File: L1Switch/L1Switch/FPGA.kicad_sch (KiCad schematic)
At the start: 4 parts, among them U1 XC7A15T-FTG256

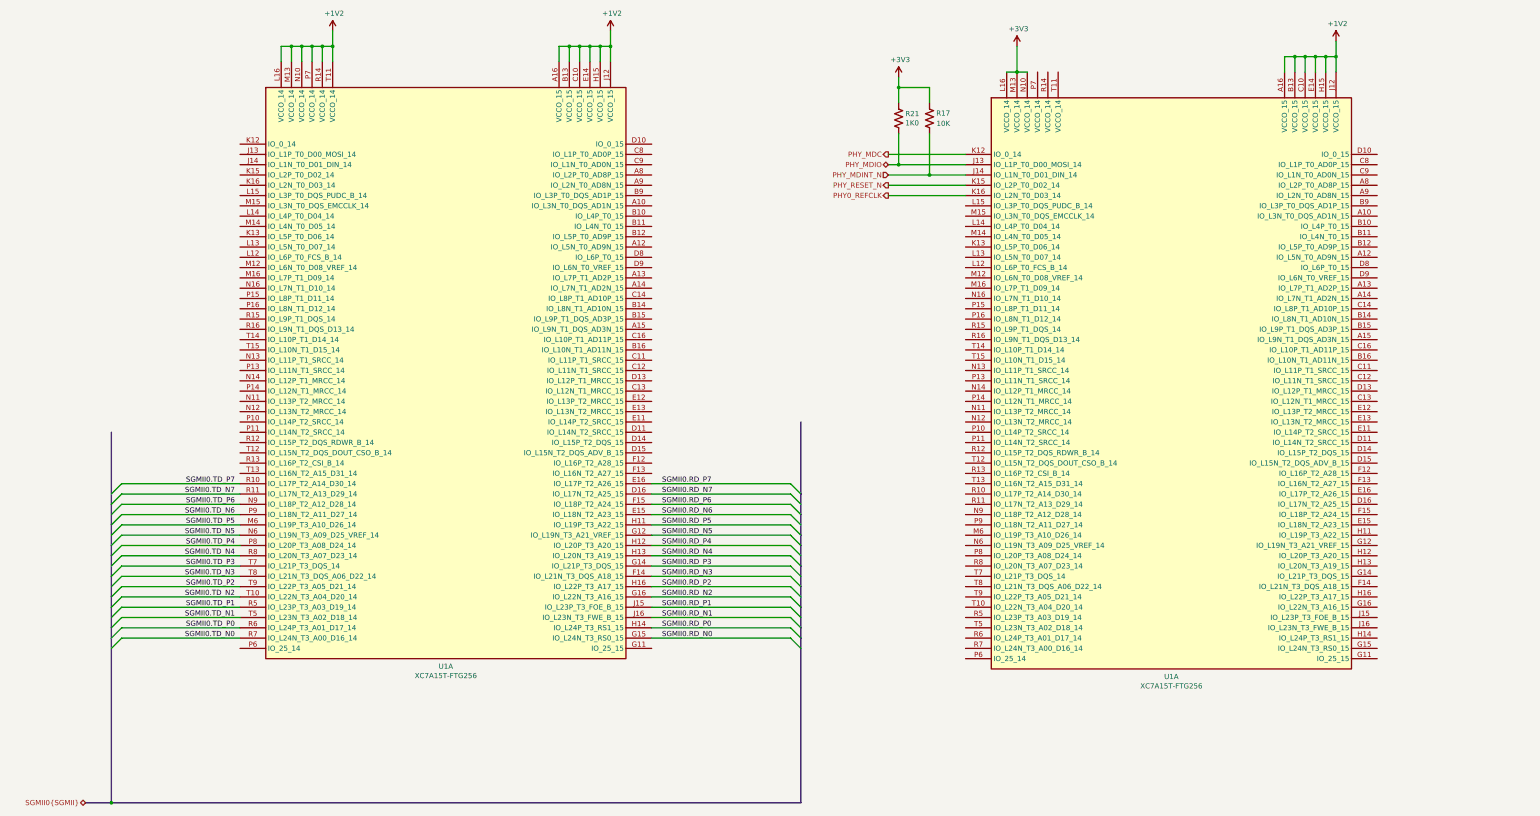
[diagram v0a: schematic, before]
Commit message: Connect/route 8 ports to PHY.
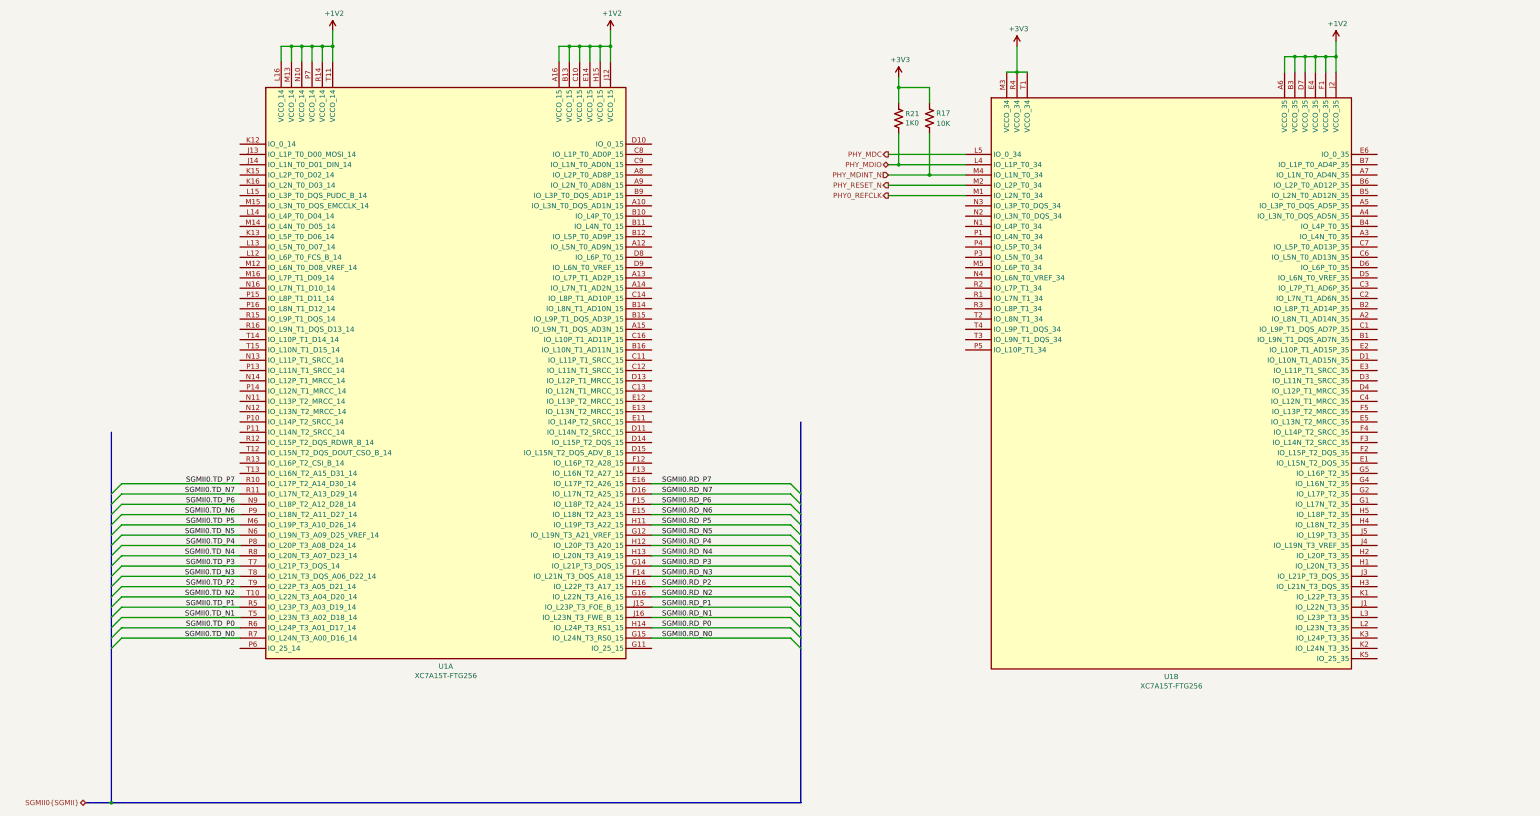
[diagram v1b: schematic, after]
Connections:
- net +1V2: now also U1.A6 (VCCO_35), U1.B3 (VCCO_35), U1.D7 (VCCO_35), U1.E4 (VCCO_35), U1.F1 (VCCO_35), U1.J2 (VCCO_35); no longer U1.A16 (VCCO_15), U1.B13 (VCCO_15), U1.C10 (VCCO_15), U1.E14 (VCCO_15), U1.H15 (VCCO_15), U1.J12 (VCCO_15)
- net +3V3: now also U1.M3 (VCCO_34), U1.R4 (VCCO_34), U1.T1 (VCCO_34); no longer U1.L16 (VCCO_14), U1.M13 (VCCO_14), U1.N10 (VCCO_14)
- net PHY0_REFCLK: now also U1.M1 (IO_L2N_T0_34); no longer U1.K16 (IO_L2N_T0_D03_14)
- net PHY_MDC: now also U1.L5 (IO_0_34); no longer U1.K12 (IO_0_14)
- net PHY_MDINT_N: now also U1.M4 (IO_L1N_T0_34); no longer U1.J14 (IO_L1N_T0_D01_DIN_14)
- net PHY_MDIO: now also U1.L4 (IO_L1P_T0_34); no longer U1.J13 (IO_L1P_T0_D00_MOSI_14)
- net PHY_RESET_N: now also U1.M2 (IO_L2P_T0_34); no longer U1.K15 (IO_L2P_T0_D02_14)
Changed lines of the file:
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@@
   (page "B")
   (bus_alias "MAC1_SGMII" (members ))
+  (junction (at 250.19 76.2))
+  (junction (at 168.91 44.45))
+  (junction (at 347.98 46.99))
+  (junction (at 171.45 44.45))
+  (junction (at 97.79 44.45))
   (junction (at 242.57 54.61))
-  (junction (at 166.37 44.45))
-  (junction (at 161.29 44.45))
-  (junction (at 97.79 44.45))
+  (junction (at 102.87 44.45))
+  (junction (at 342.9 46.99))
   (junction (at 242.57 73.66))
   (junction (at 350.52 46.99))
-  (junction (at 342.9 46.99))
+  (junction (at 166.37 44.45))
+  (junction (at 92.71 44.45))
+  (junction (at 95.25 44.45))
+  (junction (at 271.78 50.8))
+  (junction (at 161.29 44.45))
   (junction (at 100.33 44.45))
+  (junction (at 340.36 46.99))
   (junction (at 345.44 46.99))
   (junction (at 163.83 44.45))
-  (junction (at 171.45 44.45))
-  (junction (at 92.71 44.45))
-  (junction (at 168.91 44.45))
-  (junction (at 250.19 76.2))
   (junction (at 48.26 231.14))
-  (junction (at 271.78 50.8))
-  (junction (at 340.36 46.99))
-  (junction (at 95.25 44.45))
-  (junction (at 102.87 44.45))
-  (junction (at 347.98 46.99))
   (bus_entry (at 48.26 154.94) (size 2.54 -2.54))
   (bus_entry (at 48.26 157.48) (size 2.54 -2.54))
@@
   (bus (pts (xy 48.26 157.48) (xy 48.26 162.56)))
   (bus (pts (xy 48.26 162.56) (xy 48.26 167.64)))
-  (bus (pts (xy 48.26 167.64) (xy 48.26 170.18)))
-  (bus (pts (xy 48.26 170.18) (xy 48.26 175.26)))
-  (bus (pts (xy 48.26 175.26) (xy 48.26 180.34)))
-  (bus (pts (xy 48.26 180.34) (xy 48.26 182.88)))
-  (bus (pts (xy 48.26 182.88) (xy 48.26 187.96)))
-  (bus (pts (xy 48.26 187.96) (xy 48.26 190.5)))
+  (bus (pts (xy 48.26 167.64) (xy 48.26 172.72)))
+  (bus (pts (xy 48.26 172.72) (xy 48.26 177.8)))
+  (bus (pts (xy 48.26 177.8) (xy 48.26 180.34)))
+  (bus (pts (xy 48.26 180.34) (xy 48.26 185.42)))
+  (bus (pts (xy 48.26 185.42) (xy 48.26 190.5)))
   (bus (pts (xy 48.26 190.5) (xy 48.26 231.14)))
   (bus (pts (xy 48.26 231.14) (xy 218.44 231.14)))
   (bus (pts (xy 218.44 137.16) (xy 218.44 154.94)))
   (bus (pts (xy 218.44 154.94) (xy 218.44 160.02)))
-  (bus (pts (xy 218.44 160.02) (xy 218.44 165.1)))
-  (bus (pts (xy 218.44 165.1) (xy 218.44 167.64)))
+  (bus (pts (xy 218.44 160.02) (xy 218.44 162.56)))
+  (bus (pts (xy 218.44 162.56) (xy 218.44 167.64)))
   (bus (pts (xy 218.44 167.64) (xy 218.44 172.72)))
-  (bus (pts (xy 218.44 172.72) (xy 218.44 177.8)))
-  (bus (pts (xy 218.44 177.8) (xy 218.44 182.88)))
-  (bus (pts (xy 218.44 182.88) (xy 218.44 187.96)))
-  (bus (pts (xy 218.44 187.96) (xy 218.44 190.5)))
+  (bus (pts (xy 218.44 172.72) (xy 218.44 175.26)))
+  (bus (pts (xy 218.44 175.26) (xy 218.44 180.34)))
+  (bus (pts (xy 218.44 180.34) (xy 218.44 185.42)))
+  (bus (pts (xy 218.44 185.42) (xy 218.44 190.5)))
   (bus (pts (xy 218.44 190.5) (xy 218.44 231.14)))
   (label "SGMII0.TD_P7" (at 78.74 152.4 180)
@@
     )
   )
-  (symbol (lib_id "FPGA_Xilinx_Artix7:XC7A15T-FTG256") (at 130.81 121.92 0)
+  (symbol (lib_id "FPGA_Xilinx_Artix7:XC7A15T-FTG256") (at 130.81 121.92 0) (unit 1)
     (property "Reference" "U1" (id 0) (at 130.81 197.485 0))
     (property "Value" "XC7A15T-FTG256" (id 1) (at 130.81 199.7964 0))
@@
     (property "Datasheet" "" (id 3) (at 130.81 121.92 0))
   )
-  (symbol (lib_id "FPGA_Xilinx_Artix7:XC7A15T-FTG256") (at 309.88 124.46 0)
+  (symbol (lib_id "FPGA_Xilinx_Artix7:XC7A15T-FTG256") (at 309.88 124.46 0) (unit 2)
     (property "Reference" "U1" (id 0) (at 309.88 200.025 0))
     (property "Value" "XC7A15T-FTG256" (id 1) (at 309.88 202.3364 0))

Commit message: SGMII 0 Rx/Tx routed to FPGA.
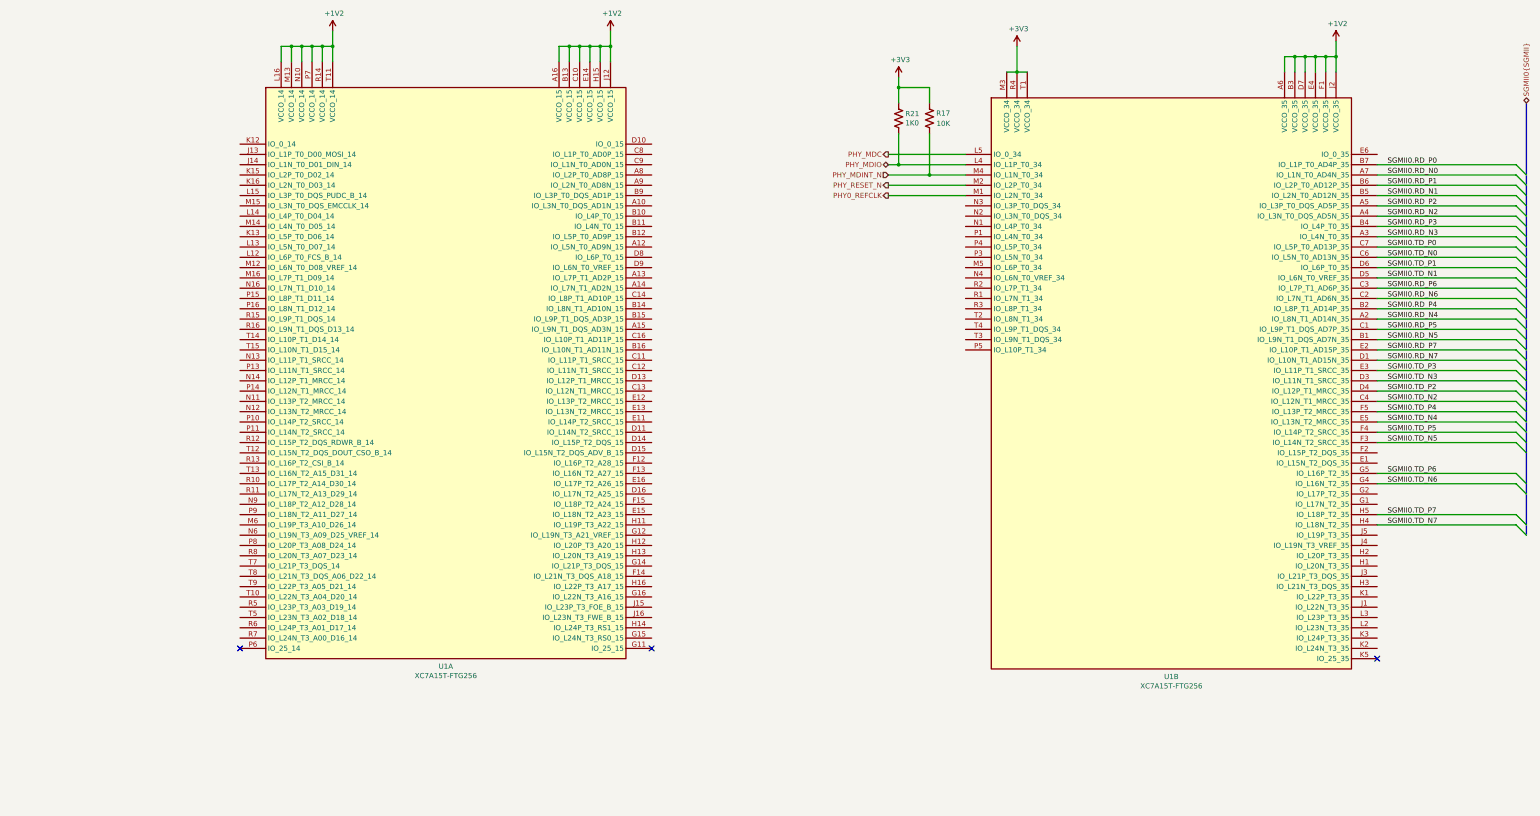
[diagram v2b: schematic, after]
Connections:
- net SGMII0.RD_N0: now also U1.A7 (IO_L1N_T0_AD4N_35); no longer U1.G15 (IO_L24N_T3_RS0_15)
- net SGMII0.RD_N1: now also U1.B5 (IO_L2N_T0_AD12N_35); no longer U1.J16 (IO_L23N_T3_FWE_B_15)
- net SGMII0.RD_N2: now also U1.A4 (IO_L3N_T0_DQS_AD5N_35); no longer U1.G16 (IO_L22N_T3_A16_15)
- net SGMII0.RD_N3: now also U1.A3 (IO_L4N_T0_35); no longer U1.F14 (IO_L21N_T3_DQS_A18_15)
- net SGMII0.RD_N4: now also U1.A2 (IO_L8N_T1_AD14N_35); no longer U1.H13 (IO_L20N_T3_A19_15)
- net SGMII0.RD_N5: now also U1.B1 (IO_L9N_T1_DQS_AD7N_35); no longer U1.G12 (IO_L19N_T3_A21_VREF_15)
- net SGMII0.RD_N6: now also U1.C2 (IO_L7N_T1_AD6N_35); no longer U1.E15 (IO_L18N_T2_A23_15)
- net SGMII0.RD_N7: now also U1.D1 (IO_L10N_T1_AD15N_35); no longer U1.D16 (IO_L17N_T2_A25_15)
- net SGMII0.RD_P0: now also U1.B7 (IO_L1P_T0_AD4P_35); no longer U1.H14 (IO_L24P_T3_RS1_15)
- net SGMII0.RD_P1: now also U1.B6 (IO_L2P_T0_AD12P_35); no longer U1.J15 (IO_L23P_T3_FOE_B_15)
- net SGMII0.RD_P2: now also U1.A5 (IO_L3P_T0_DQS_AD5P_35); no longer U1.H16 (IO_L22P_T3_A17_15)
- net SGMII0.RD_P3: now also U1.B4 (IO_L4P_T0_35); no longer U1.G14 (IO_L21P_T3_DQS_15)
- net SGMII0.RD_P4: now also U1.B2 (IO_L8P_T1_AD14P_35); no longer U1.H12 (IO_L20P_T3_A20_15)
- net SGMII0.RD_P5: now also U1.C1 (IO_L9P_T1_DQS_AD7P_35); no longer U1.H11 (IO_L19P_T3_A22_15)
- net SGMII0.RD_P6: now also U1.C3 (IO_L7P_T1_AD6P_35); no longer U1.F15 (IO_L18P_T2_A24_15)
- net SGMII0.RD_P7: now also U1.E2 (IO_L10P_T1_AD15P_35); no longer U1.E16 (IO_L17P_T2_A26_15)
- net SGMII0.TD_N0: now also U1.C6 (IO_L5N_T0_AD13N_35); no longer U1.R7 (IO_L24N_T3_A00_D16_14)
- net SGMII0.TD_N1: now also U1.D5 (IO_L6N_T0_VREF_35); no longer U1.T5 (IO_L23N_T3_A02_D18_14)
- net SGMII0.TD_N2: now also U1.C4 (IO_L12N_T1_MRCC_35); no longer U1.T10 (IO_L22N_T3_A04_D20_14)
- net SGMII0.TD_N3: now also U1.D3 (IO_L11N_T1_SRCC_35); no longer U1.T8 (IO_L21N_T3_DQS_A06_D22_14)
- net SGMII0.TD_N4: now also U1.E5 (IO_L13N_T2_MRCC_35); no longer U1.R8 (IO_L20N_T3_A07_D23_14)
- net SGMII0.TD_N5: now also U1.F3 (IO_L14N_T2_SRCC_35); no longer U1.N6 (IO_L19N_T3_A09_D25_VREF_14)
- net SGMII0.TD_N6: now also U1.G4 (IO_L16N_T2_35); no longer U1.P9 (IO_L18N_T2_A11_D27_14)
- net SGMII0.TD_N7: now also U1.H4 (IO_L18N_T2_35); no longer U1.R11 (IO_L17N_T2_A13_D29_14)
- net SGMII0.TD_P0: now also U1.C7 (IO_L5P_T0_AD13P_35); no longer U1.R6 (IO_L24P_T3_A01_D17_14)
- net SGMII0.TD_P1: now also U1.D6 (IO_L6P_T0_35); no longer U1.R5 (IO_L23P_T3_A03_D19_14)
- net SGMII0.TD_P2: now also U1.D4 (IO_L12P_T1_MRCC_35); no longer U1.T9 (IO_L22P_T3_A05_D21_14)
- net SGMII0.TD_P3: now also U1.E3 (IO_L11P_T1_SRCC_35); no longer U1.T7 (IO_L21P_T3_DQS_14)
- net SGMII0.TD_P4: now also U1.F5 (IO_L13P_T2_MRCC_35); no longer U1.P8 (IO_L20P_T3_A08_D24_14)
- net SGMII0.TD_P5: now also U1.F4 (IO_L14P_T2_SRCC_35); no longer U1.M6 (IO_L19P_T3_A10_D26_14)
- net SGMII0.TD_P6: now also U1.G5 (IO_L16P_T2_35); no longer U1.N9 (IO_L18P_T2_A12_D28_14)
- net SGMII0.TD_P7: now also U1.H5 (IO_L18P_T2_35); no longer U1.R10 (IO_L17P_T2_A14_D30_14)
- no-connect marks 0 -> 3

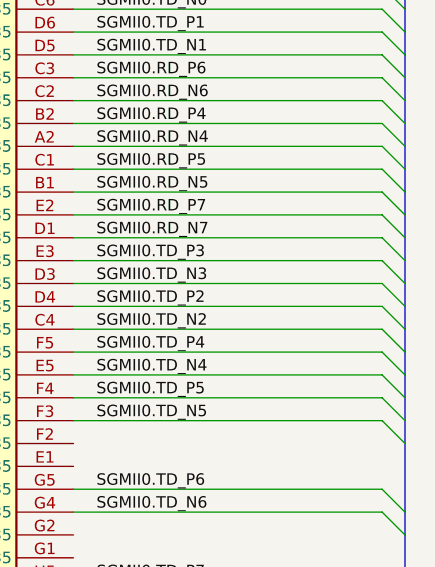
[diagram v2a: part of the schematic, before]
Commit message: Add decoupling caps and ferrite bead. Clean up reference designators.
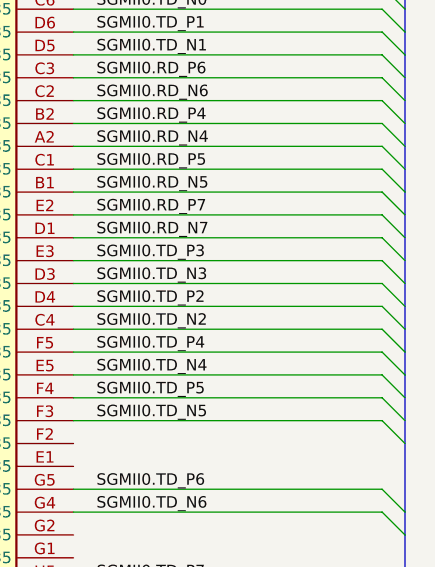
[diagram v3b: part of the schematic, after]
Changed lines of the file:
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@@
   (page "B")
   (bus_alias "MAC1_SGMII" (members ))
+  (junction (at 347.98 46.99))
+  (junction (at 168.91 44.45))
+  (junction (at 345.44 46.99))
+  (junction (at 271.78 50.8))
+  (junction (at 163.83 44.45))
+  (junction (at 250.19 76.2))
   (junction (at 242.57 54.61))
-  (junction (at 168.91 44.45))
+  (junction (at 97.79 44.45))
+  (junction (at 95.25 44.45))
+  (junction (at 166.37 44.45))
+  (junction (at 242.57 73.66))
+  (junction (at 100.33 44.45))
+  (junction (at 171.45 44.45))
+  (junction (at 340.36 46.99))
+  (junction (at 342.9 46.99))
+  (junction (at 350.52 46.99))
   (junction (at 92.71 44.45))
-  (junction (at 342.9 46.99))
-  (junction (at 345.44 46.99))
-  (junction (at 242.57 73.66))
-  (junction (at 97.79 44.45))
+  (junction (at 161.29 44.45))
   (junction (at 102.87 44.45))
-  (junction (at 95.25 44.45))
-  (junction (at 171.45 44.45))
-  (junction (at 350.52 46.99))
-  (junction (at 161.29 44.45))
-  (junction (at 250.19 76.2))
-  (junction (at 347.98 46.99))
-  (junction (at 271.78 50.8))
-  (junction (at 166.37 44.45))
-  (junction (at 100.33 44.45))
-  (junction (at 163.83 44.45))
-  (junction (at 340.36 46.99))
+  (no_connect (at 181.61 193.04))
   (no_connect (at 80.01 193.04))
-  (no_connect (at 181.61 193.04))
   (no_connect (at 360.68 195.58))
   (bus_entry (at 394.97 73.66) (size 2.54 2.54))
@@
   (bus (pts (xy 397.51 111.76) (xy 397.51 116.84)))
   (bus (pts (xy 397.51 116.84) (xy 397.51 121.92)))
-  (bus (pts (xy 397.51 121.92) (xy 397.51 127)))
-  (bus (pts (xy 397.51 127) (xy 397.51 132.08)))
+  (bus (pts (xy 397.51 121.92) (xy 397.51 124.46)))
+  (bus (pts (xy 397.51 124.46) (xy 397.51 129.54)))
+  (bus (pts (xy 397.51 129.54) (xy 397.51 132.08)))
   (bus (pts (xy 397.51 132.08) (xy 397.51 137.16)))
   (bus (pts (xy 397.51 137.16) (xy 397.51 142.24)))

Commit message: Layout replicated to Net2.
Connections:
- net PHY_MDC renamed PHY_MDC0
- net PHY_MDIO renamed PHY_MDIO0
